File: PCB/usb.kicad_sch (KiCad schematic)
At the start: 7 parts

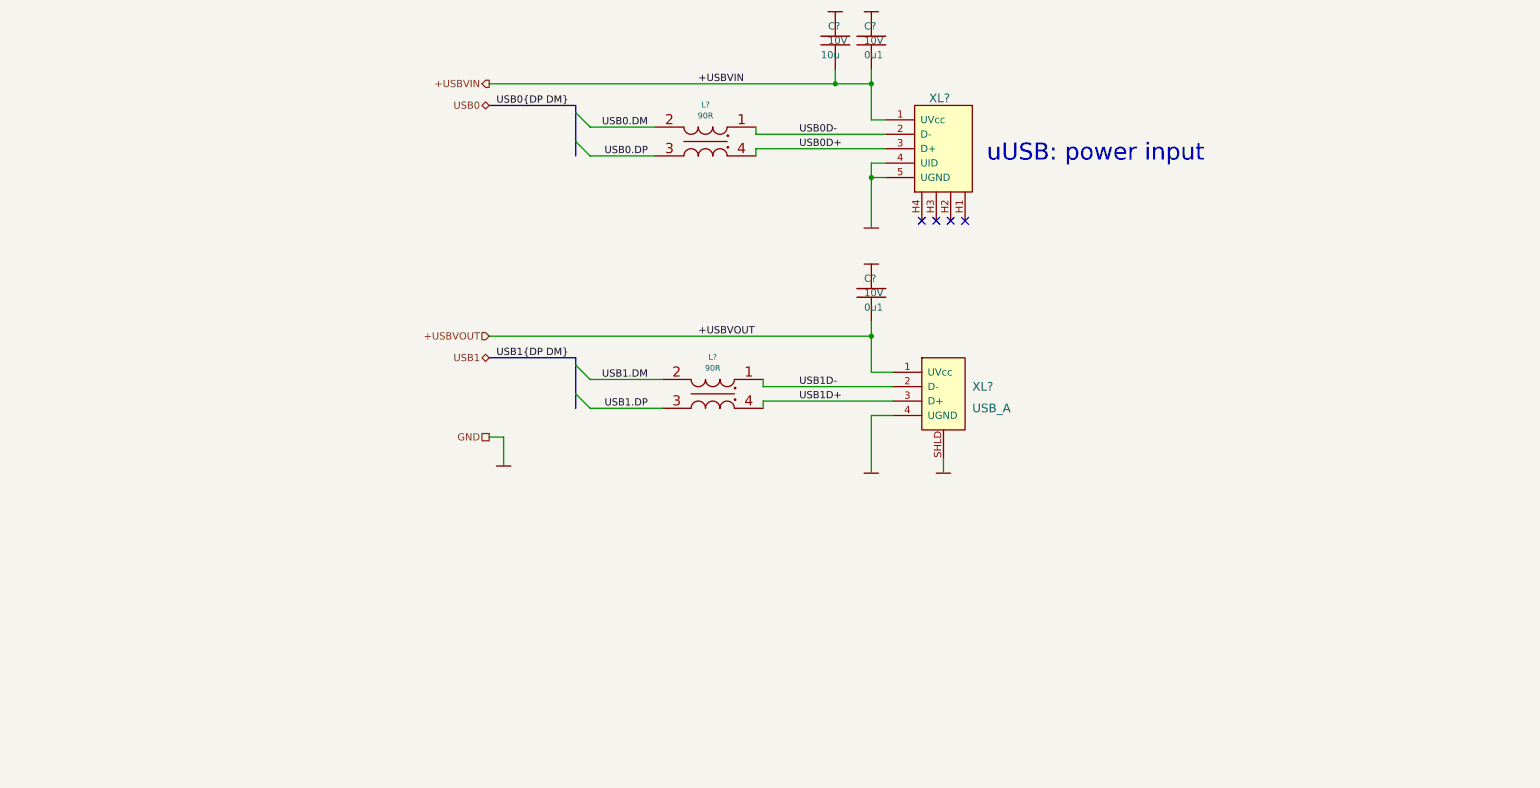
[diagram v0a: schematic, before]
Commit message: + LCD
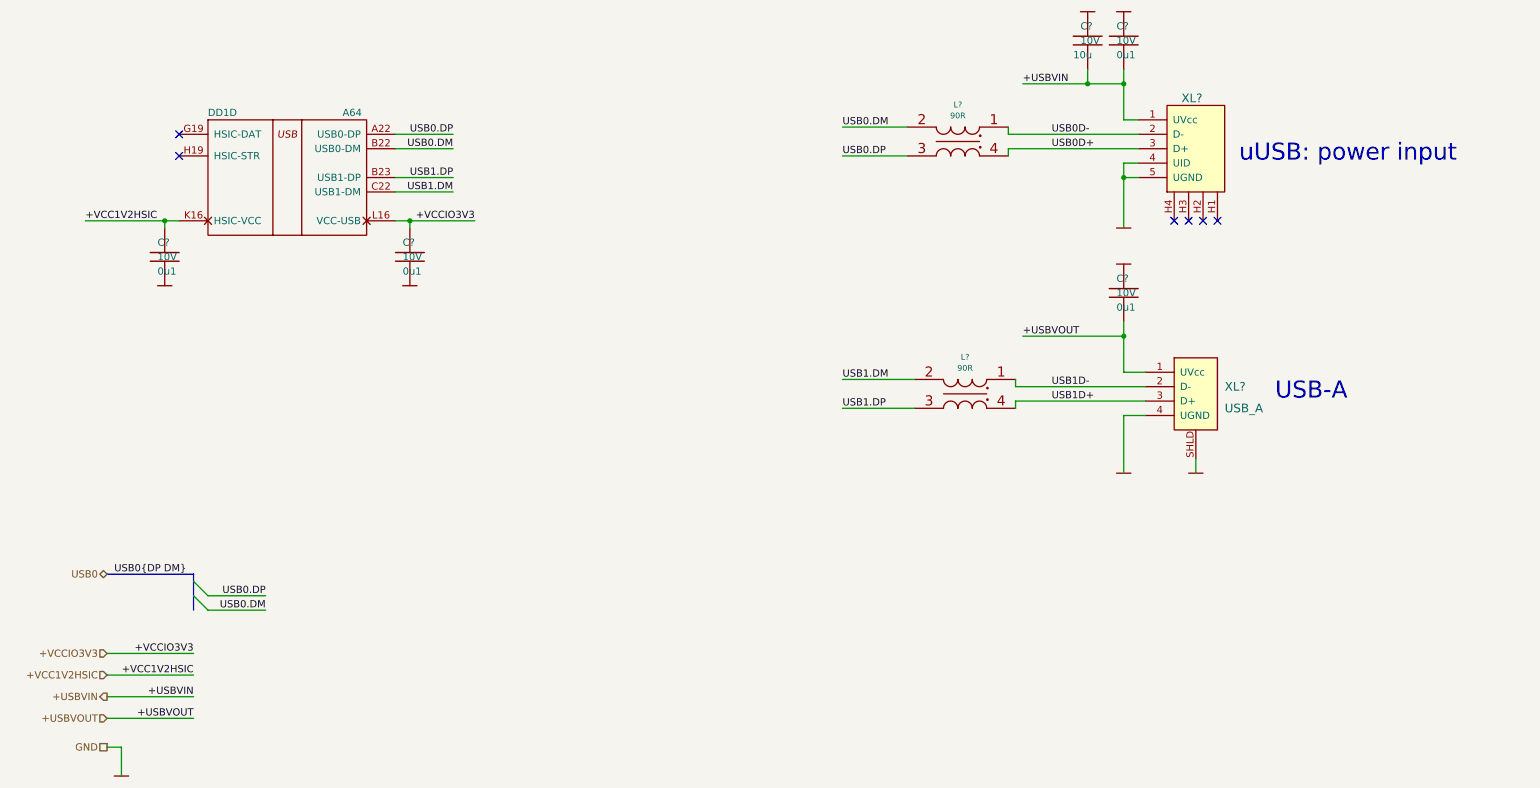
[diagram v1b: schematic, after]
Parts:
- added C? (x2): 0u1, Capacitors:CAP_0402, symbol Tittar_kl:C
- added DD1: A64, BGA:BGA-529_23x23_15.0x15.0mm, symbol Allwinner:A64
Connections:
- net GND: now also C?.1, C?.1
- net USB0.DM: now also DD1.B22 (USB0-DM)
- net USB0.DP: now also DD1.A22 (USB0-DP)
- net USB1.DM: now also DD1.C22 (USB1-DM)
- net USB1.DP: now also DD1.B23 (USB1-DP)
- new net +VCC1V2HSIC: C?.2, DD1.K16 (HSIC-VCC)
- new net +VCCIO3V3: C?.2, DD1.L16 (VCC-USB)
- no-connect marks 4 -> 6
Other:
- note added: "USB-A"
- moved on the sheet: C?, L?, XL?

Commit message: Before eMMC removing
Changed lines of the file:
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@@
   (no_connect (at 224.79 93.98))
   (no_connect (at 222.25 93.98))
-  (bus_entry (at 46.99 160.02) (size 2.54 2.54)
-    (stroke (width 0) (type default) (color 0 0 0 0))
-  )
-  (bus_entry (at 46.99 157.48) (size 2.54 2.54)
-    (stroke (width 0) (type default) (color 0 0 0 0))
-  )
   (wire (pts (xy 161.29 127) (xy 173.99 127))
     (stroke (width 0) (type default) (color 0 0 0 0))
@@
     (stroke (width 0) (type default) (color 0 0 0 0))
   )
-  (bus (pts (xy 46.99 160.02) (xy 46.99 162.56))
-    (stroke (width 0) (type default) (color 0 0 0 0))
-  )
   (wire (pts (xy 210.82 95.25) (xy 210.82 86.36))
     (stroke (width 0) (type default) (color 0 0 0 0))
@@
   )
   (wire (pts (xy 214.63 120.65) (xy 210.82 120.65))
-    (stroke (width 0) (type default) (color 0 0 0 0))
-  )
-  (bus (pts (xy 46.99 157.48) (xy 46.99 160.02))
     (stroke (width 0) (type default) (color 0 0 0 0))
   )
@@
     (stroke (width 0) (type default) (color 0 0 0 0))
   )
-  (wire (pts (xy 49.53 162.56) (xy 59.69 162.56))
-    (stroke (width 0) (type default) (color 0 0 0 0))
-  )
   (wire (pts (xy 85.09 93.98) (xy 85.09 95.25))
     (stroke (width 0) (type default) (color 0 0 0 0))
@@
   )
   (wire (pts (xy 82.55 86.36) (xy 92.71 86.36))
-    (stroke (width 0) (type default) (color 0 0 0 0))
-  )
-  (wire (pts (xy 49.53 160.02) (xy 59.69 160.02))
-    (stroke (width 0) (type default) (color 0 0 0 0))
-  )
-  (bus (pts (xy 46.99 156.21) (xy 46.99 157.48))
     (stroke (width 0) (type default) (color 0 0 0 0))
   )
@@
     (effects (font (size 1.27 1.27)) (justify right bottom))
   )
-  (label "USB0{DP DM}" (at 33.02 156.21 0)
-    (effects (font (size 1.27 1.27)) (justify left bottom))
+  (label "USB0{DP DM}" (at 46.99 156.21 180)
+    (effects (font (size 1.27 1.27)) (justify right bottom))
   )
   (label "USB1D+" (at 198.12 125.73 0)
@@
     (effects (font (size 1.27 1.27)) (justify left bottom))
   )
-  (label "USB0.DP" (at 59.69 160.02 180)
-    (effects (font (size 1.27 1.27)) (justify right bottom))
-  )
   (label "USB0.DP" (at 92.71 78.74 180)
     (effects (font (size 1.27 1.27)) (justify right bottom))
   )
-  (label "USB0.DM" (at 59.69 162.56 180)
-    (effects (font (size 1.27 1.27)) (justify right bottom))
-  )
   (label "USB0.DP" (at 161.29 82.55 0)
     (effects (font (size 1.27 1.27)) (justify left bottom))
@@
     (effects (font (size 1.27 1.27)) (justify right))
   )
-  (symbol (lib_name "A64_3") (lib_id "Allwinner:A64") (at 77.47 76.2 0) (unit 4)
+  (symbol (lib_id "Allwinner:A64") (at 77.47 76.2 0) (unit 4)
     (in_bom yes) (on_board yes)
     (property "Reference" "DD1" (id 0) (at 52.07 74.93 0))
